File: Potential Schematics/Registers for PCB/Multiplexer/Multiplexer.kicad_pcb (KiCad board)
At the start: 2 copper layers, 162.6 x 137.2 mm, 94 parts, among them J1 Conn_01x40_Female, J2 Conn_01x08_Female, J3 Conn_01x08_Female, J4 Conn_01x08_Female, J5 Conn_01x08_Female, J6 Conn_01x04_Female, U1 74LS04, U10 74LS32, U11 74LS32, U12 74LS32, U13 74LS32, U14 74LS08, U15 74LS08, U16 74LS08, U17 74LS08, U18 74LS08, U19 74LS08, U2 74LS08, U20 74LS08, U21 74LS08, U22 74LS08, U23 74LS08, U24 74LS08, U25 74LS04, U26 74LS08, U27 74LS08, U28 74LS08, U29 74LS08, U3 74LS08, U30 74LS08, U31 74LS08, U32 74LS08, U33 74LS08, U34 74LS32, U35 74LS32, U36 74LS32, U37 74LS32, U38 74LS08, U39 74LS08, U4 74LS08, U40 74LS08, U41 74LS08, U42 74LS08, U43 74LS08, U44 74LS08, U45 74LS08, U46 74LS04, U47 74LS08, U48 74LS08, U49 74LS08, U5 74LS08, U50 74LS08, U51 74LS08, U52 74LS08, U53 74LS08, U54 74LS08, U55 74LS32, U56 74LS32, U57 74LS32, U58 74LS32, U59 74LS08, U6 74LS08, U60 74LS08, U61 74LS08, U62 74LS08, U63 74LS08, U64 74LS08, U65 74LS08, U66 74LS08, U67 74LS04, U68 74LS08, U69 74LS08, U7 74LS08, U70 74LS08, U71 74LS08, U72 74LS08, U73 74LS08, U74 74LS08, U75 74LS08, U76 74LS32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

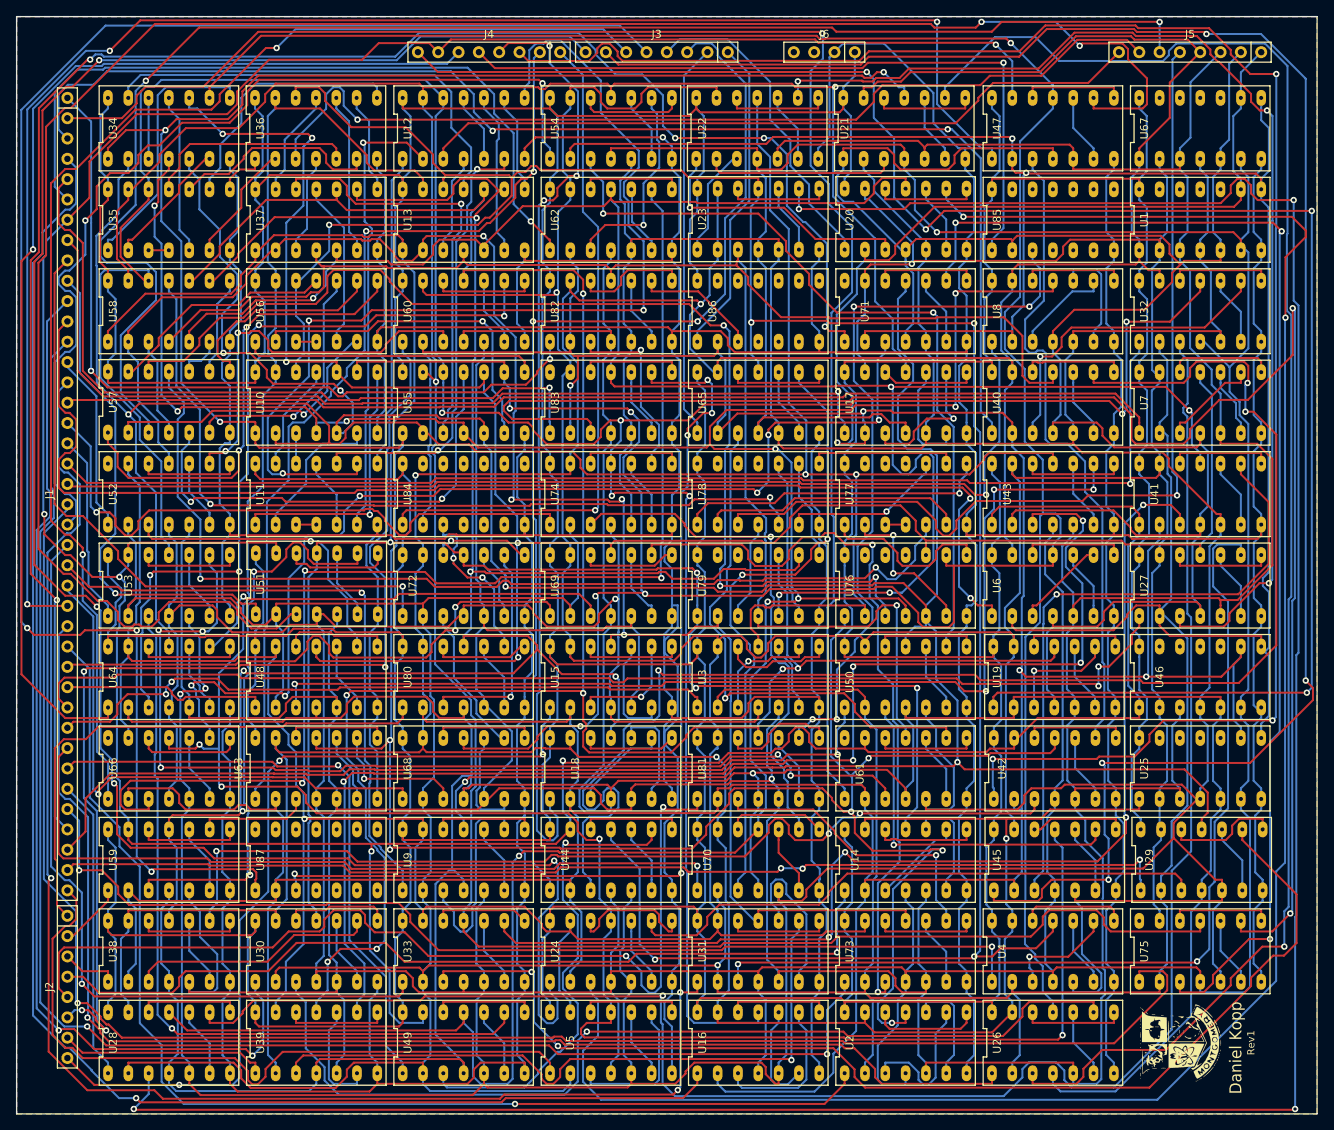
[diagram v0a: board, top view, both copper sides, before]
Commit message: Updated PCB and is ready to be ordered
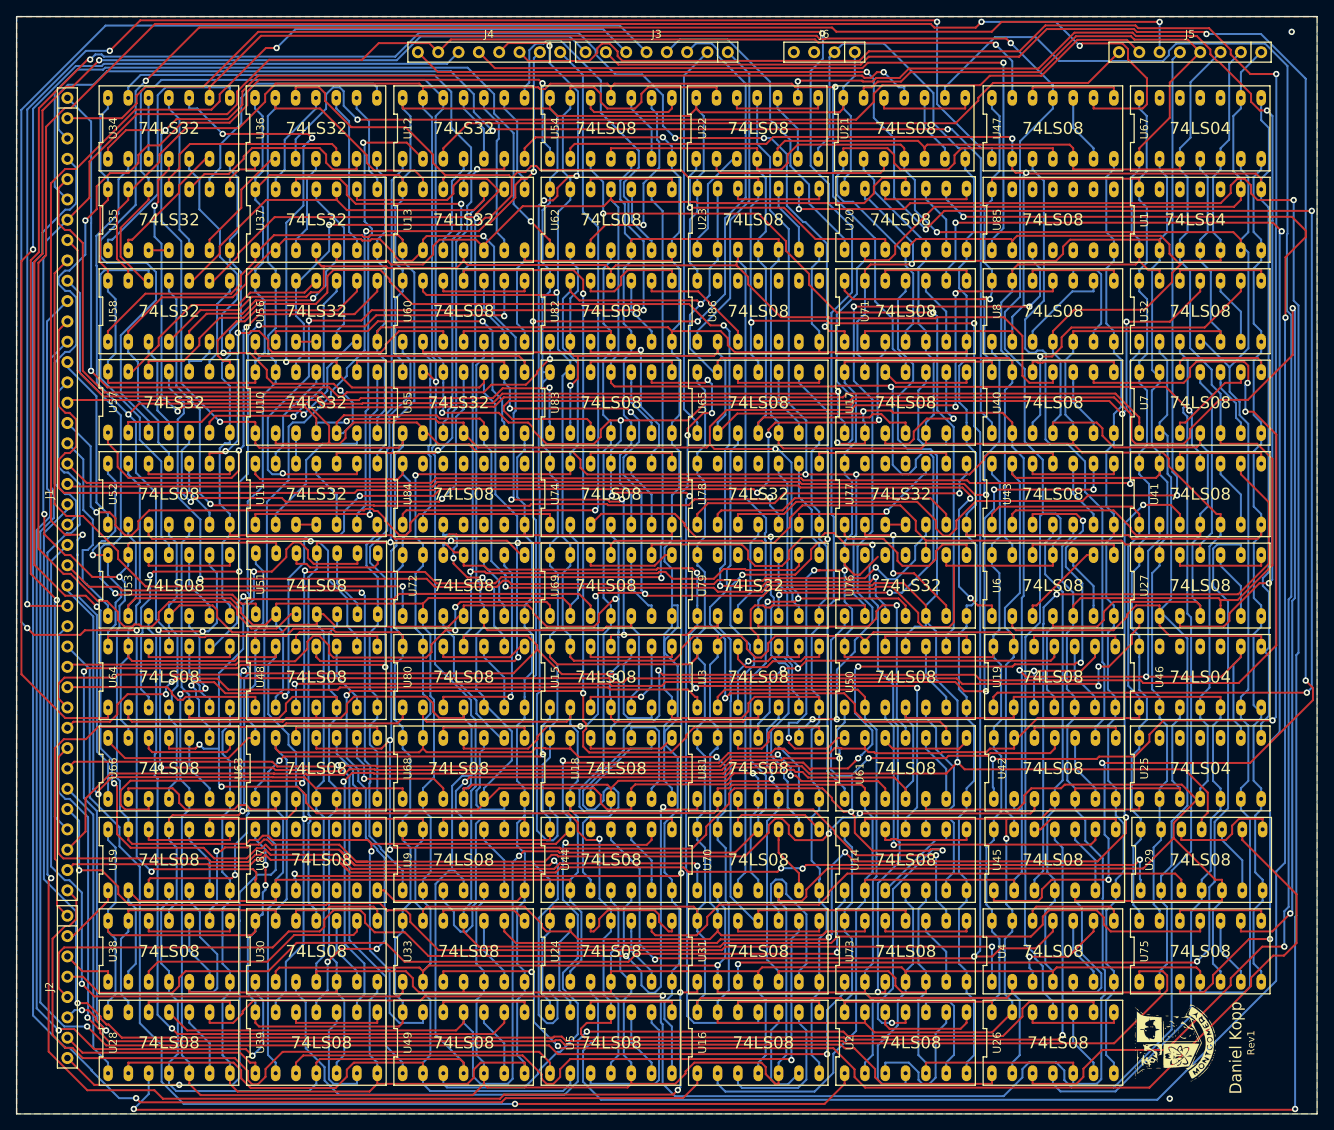
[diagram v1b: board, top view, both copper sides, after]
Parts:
- moved G*** 0.64 mm to (177.2, 156.8)
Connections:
- U52 pad 14: Net-(U52-Pad14) -> VCC
- U61 pad 14: Net-(U61-Pad14) -> VCC
- U66 pad 14: Net-(U66-Pad14) -> VCC
- U71 pad 14: Net-(U71-Pad14) -> VCC
- U75 pad 14: Net-(U75-Pad14) -> VCC
- U83 pad 14: Net-(U83-Pad14) -> VCC
- U87 pad 14: (no net) -> VCC
- U87 pad 7: (no net) -> GND
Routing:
- net VCC: track 1142.4 -> 1268.2 mm, vias 0 -> 7
- net GND: track 1230.7 -> 1250.4 mm, vias 1 -> 3
- net /64:4 Multiplexer/Dc0: track 254.2 -> 258.8 mm
- net Net-(U39-Pad9): track 163.1 -> 166.5 mm
- net Net-(U38-Pad9): track 119.7 -> 122.1 mm
- net /64:4 Multiplexer/D13: track 97.8 -> 99.8 mm
- net /64:4 Multiplexer/D01: track 139.8 -> 141.7 mm
- net /64:4 Multiplexer/Dc2: track 161.8 -> 163.7 mm
- net /64:4 Multiplexer/Da0: track 104.5 -> 106.4 mm
- net /64:4 Multiplexer/D81: track 469.5 -> 468.0 mm
- net /64:4 Multiplexer/D52: track 23.7 -> 25.1 mm
- net /64:4 Multiplexer/D72: track 62.5 -> 63.9 mm
- net Net-(U51-Pad9): track 71.3 -> 70.1 mm
- net Net-(U61-Pad12): track 12.8 -> 11.7 mm
- net /64:4 Multiplexer/16;1_Multiplexer/Sheet5BB0E1EE/D3: track 402.3 -> 403.2 mm
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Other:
- board text added: "74LS04"
- board text added: "74LS08"
- board text added: "74LS32"
